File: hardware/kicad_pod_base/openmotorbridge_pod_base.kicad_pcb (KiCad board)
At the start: 2 copper layers, 36 x 20 mm, 6 parts, among them J1 MILL_MAX_824_SMD_6P, J2 M8_6PIN_RECEPTACLE, U1 SP3012-06UTG

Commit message: feat(hardware): implement mechanical Poka-Yoke anti-rotation key for pod base PCB and bulkhead
- Added 4.0 x 2.5 mm asymmetric keying notch to the bottom edge of openmotorbridge_pod_base (X=125..129mm) in Edge.Cuts.
- Added silkscreen alignment markings '▲ TOP / OBEN' and '▼ POKA-YOKE KEY'.
- Added matching 1.8 x 3.0 x 3.0 mm Poka-Yoke alignment lug in 002_pod_bulkhead_partition.scad.
- Preserved all existing 100% autorouted copper tracks, vias, and pad netlists.
- Verified 0 unconnected items and 0 clearance errors in KiCad DRC.
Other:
- outline, holes or cut-outs redrawn
- board text added: "▲ TOP / OBEN"
- board text added: "▼ POKA-YOKE KEY"
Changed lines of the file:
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@@
 	(gr_line
 		(start 134 90)
+		(end 129 90)
+		(stroke
+			(width 0.15)
+			(type solid)
+		)
+		(layer "Edge.Cuts")
+	)
+	(gr_line
+		(start 129 90)
+		(end 129 87.5)
+		(stroke
+			(width 0.15)
+			(type solid)
+		)
+		(layer "Edge.Cuts")
+	)
+	(gr_line
+		(start 129 87.5)
+		(end 125 87.5)
+		(stroke
+			(width 0.15)
+			(type solid)
+		)
+		(layer "Edge.Cuts")
+	)
+	(gr_line
+		(start 125 87.5)
+		(end 125 90)
+		(stroke
+			(width 0.15)
+			(type solid)
+		)
+		(layer "Edge.Cuts")
+	)
+	(gr_line
+		(start 125 90)
 		(end 102 90)
 		(stroke
@@
 		(layer "Edge.Cuts")
 	)
+	(gr_text "▲ TOP / OBEN"
+		(at 127 72 0)
+		(layer "F.SilkS")
+		(effects
+			(font
+				(size 0.45 0.45)
+				(thickness 0.09)
+			)
+		)
+	)
+	(gr_text "▼ POKA-YOKE KEY"
+		(at 127 86.2 0)
+		(layer "F.SilkS")
+		(effects
+			(font
+				(size 0.4 0.4)
+				(thickness 0.08)
+			)
+		)
+	)
 	(gr_line

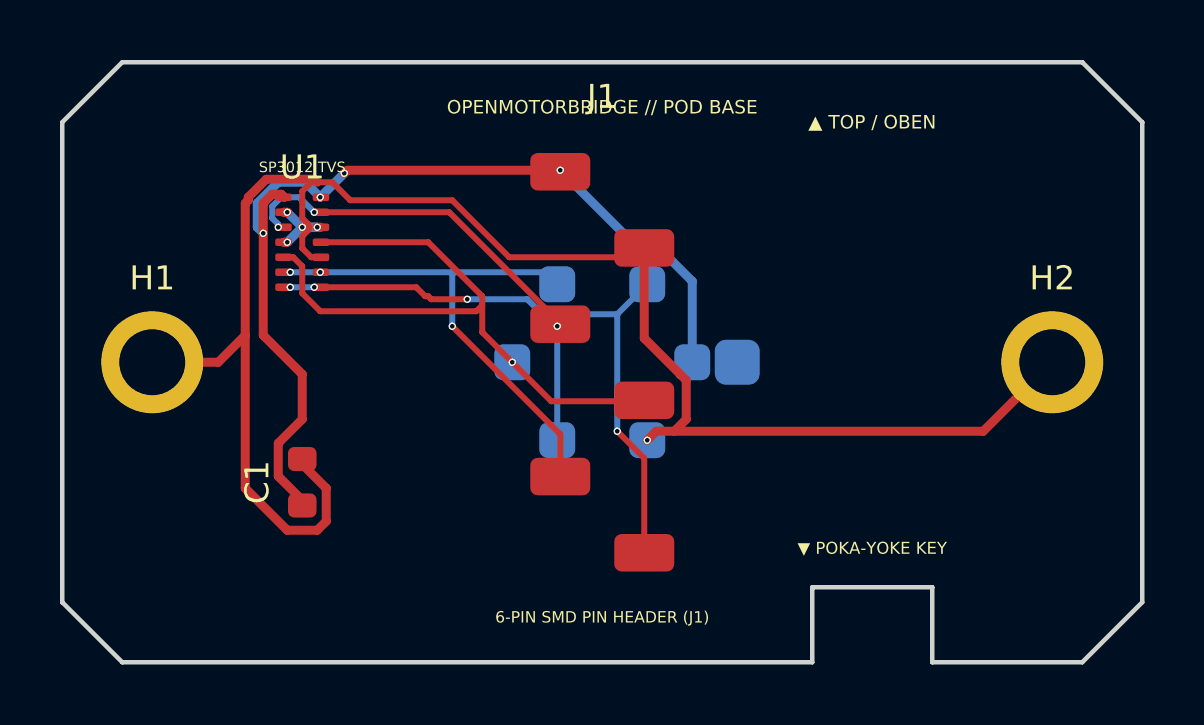
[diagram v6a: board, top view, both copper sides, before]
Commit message: feat(hardware): implement dual-port pod base, magsafe frame dock, and saddlebag split grommet
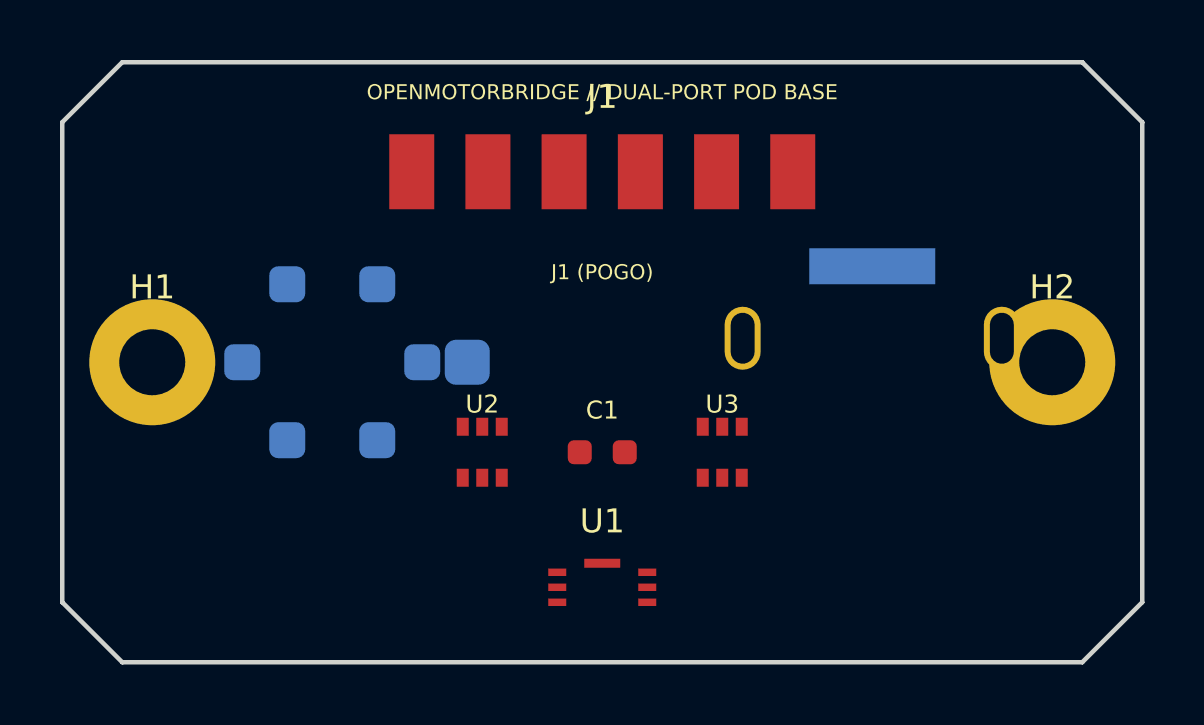
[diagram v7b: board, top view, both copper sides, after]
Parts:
- added J3: PORT_B_USBC_SLIM, Connector_USB:USB_C_Receptacle_HRO_TYPE-C-31-M-12, B.Cu at (127.0, 80.0)
- added U2: LM66100_PORTA, Package_TO_SOT_SMD:SOT-363_SC-70-6, F.Cu at (114.0, 83.0)
- added U3: LM66100_PORTB, Package_TO_SOT_SMD:SOT-363_SC-70-6, F.Cu at (122.0, 83.0)
- H1, H2: value M2_MountingHole -> MountingHole_M2_Pad
- J1: value MILL_MAX_824_SMD_6P -> MILL_MAX_824_POGO_6P
- J2: value M8_6PIN_RECEPTACLE -> PORT_A_M8_6PIN
- moved U1 15.2 mm to (118.0, 87.5)
- moved C1 10.0 mm to (118.0, 83.0), turned to 0 degrees
- moved J2 9.00 mm to (109.0, 80.0)
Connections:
- J2 pad 1: VCC -> VCC_M8
- U1 pad 2: GND -> SIG_P
- U1 pad 3: SIG_P -> SIG_N
- U1 pad 5: SIG_N -> TRIGGER_PPS
- U1 pad 6: TRIGGER_PPS -> 1WIRE_ID
- U1 pad 7: 1WIRE_ID -> GND
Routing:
- net GND: track 61.3 -> 0.00 mm, vias 5 -> 0
- net VCC: track 32.9 -> 0.00 mm, vias 4 -> 0
- net SIG_N: track 21.7 -> 0.00 mm, vias 1 -> 0
- net 1WIRE_ID: track 21.4 -> 0.00 mm, vias 4 -> 0
- net TRIGGER_PPS: track 17.6 -> 0.00 mm, vias 3 -> 0
- net SIG_P: track 16.5 -> 0.00 mm, vias 3 -> 0
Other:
- outline, holes or cut-outs redrawn
- board text added: "J1 (POGO)"
- board text added: "OPENMOTORBRIDGE // DUAL-PORT POD BASE"
- board text added: "PORT A (M8)"
- board text added: "PORT B (USB-C)"
- board text removed: "6-PIN SMD PIN HEADER (J1)"
- board text removed: "M8 6-PIN IP67 PANEL RECEPTACLE (J2)"
- board text removed: "OPENMOTORBRIDGE // POD BASE"
- board text removed: "OPENMOTORBRIDGE // POD BASE (REAR)"
- board text removed: "SP3012 TVS"
- board text removed: "▲ TOP / OBEN"
- board text removed: "▼ POKA-YOKE KEY"

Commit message: fix(hardware): restore exact vertical J1 pogo header footprint and add photorealistic 3D STEP models
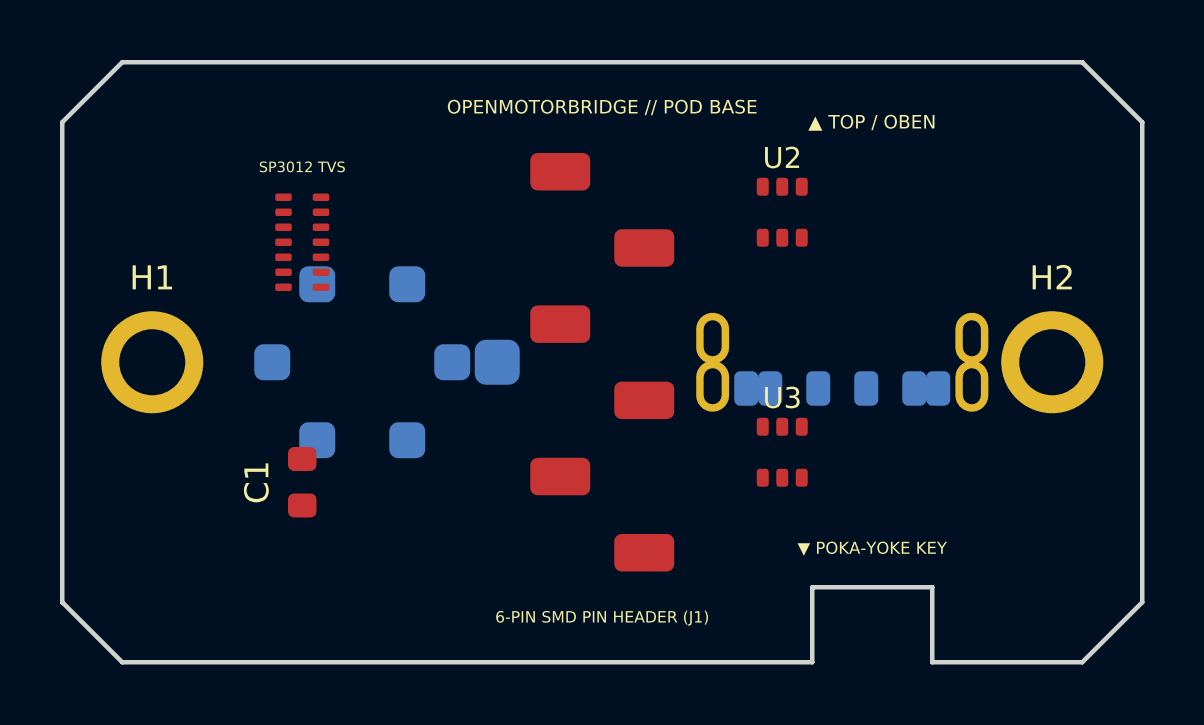
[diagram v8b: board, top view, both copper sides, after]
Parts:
- H1, H2: value MountingHole_M2_Pad -> M2_MountingHole
- J1: value MILL_MAX_824_POGO_6P -> MILL_MAX_824_SMD_6P
- J3: footprint Connector_USB:USB_C_Receptacle_HRO_TYPE-C-31-M-12 -> Connector_USB:USB_C_Receptacle_GCT_USB4125-xx-x_6P_TopMnt_Horizontal
- moved U1 15.2 mm to (108.0, 76.0)
- moved U2 12.8 mm to (124.0, 75.0)
- moved C1 10.0 mm to (108.0, 84.0), turned to 90 degrees
- moved U3 2.00 mm to (124.0, 83.0)
- moved J2 1.00 mm to (110.0, 80.0)
- moved J3 1.00 mm to (126.0, 80.0), turned to 180 degrees
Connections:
- U1 pad 2: SIG_P -> GND
- U1 pad 3: SIG_N -> SIG_P
- U1 pad 5: TRIGGER_PPS -> SIG_N
- U1 pad 6: 1WIRE_ID -> TRIGGER_PPS
- U1 pad 7: GND -> 1WIRE_ID
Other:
- outline, holes or cut-outs redrawn
- board text added: "6-PIN SMD PIN HEADER (J1)"
- board text added: "OPENMOTORBRIDGE // POD BASE"
- board text added: "OPENMOTORBRIDGE // POD BASE (REAR)"
- board text added: "PORT A (M8) // PORT B (USB-C) DUAL-PORT"
- board text added: "SP3012 TVS"
- board text added: "▲ TOP / OBEN"
- board text added: "▼ POKA-YOKE KEY"
- board text removed: "J1 (POGO)"
- board text removed: "OPENMOTORBRIDGE // DUAL-PORT POD BASE"
- board text removed: "PORT A (M8)"
- board text removed: "PORT B (USB-C)"
